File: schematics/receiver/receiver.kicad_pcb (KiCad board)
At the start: 4 copper layers, 30.6 x 67.9 mm, 28 parts, among them M1 Servo, M2 Motor, Q1 2N7000, Q2 2N7000, Q3 2N7000, Q4 2N7000, SW1 SW_Nidec_CAS-120A1, U1 PIC16F18324-xSL, U2 LM2937xT, U3 NRF24L01_Breakout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

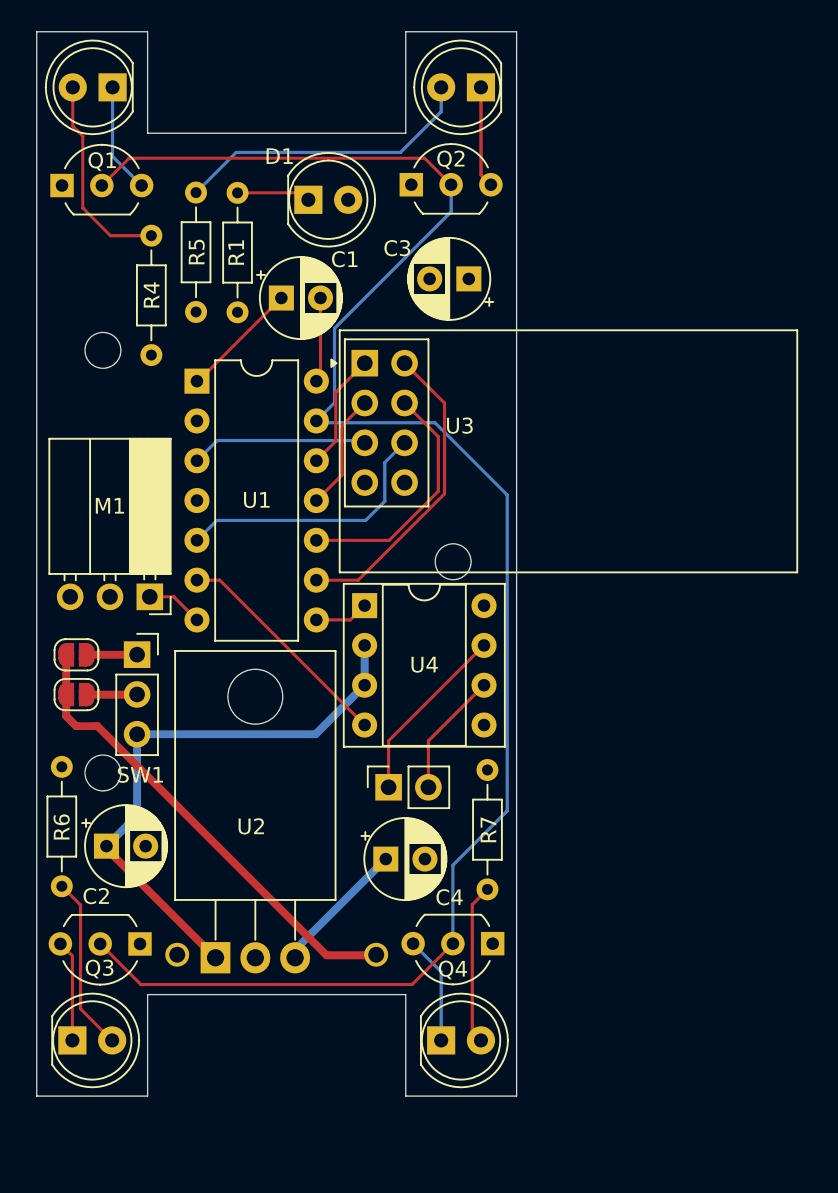
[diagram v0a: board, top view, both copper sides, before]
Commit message: Change mcu type select to be pull down for RX board
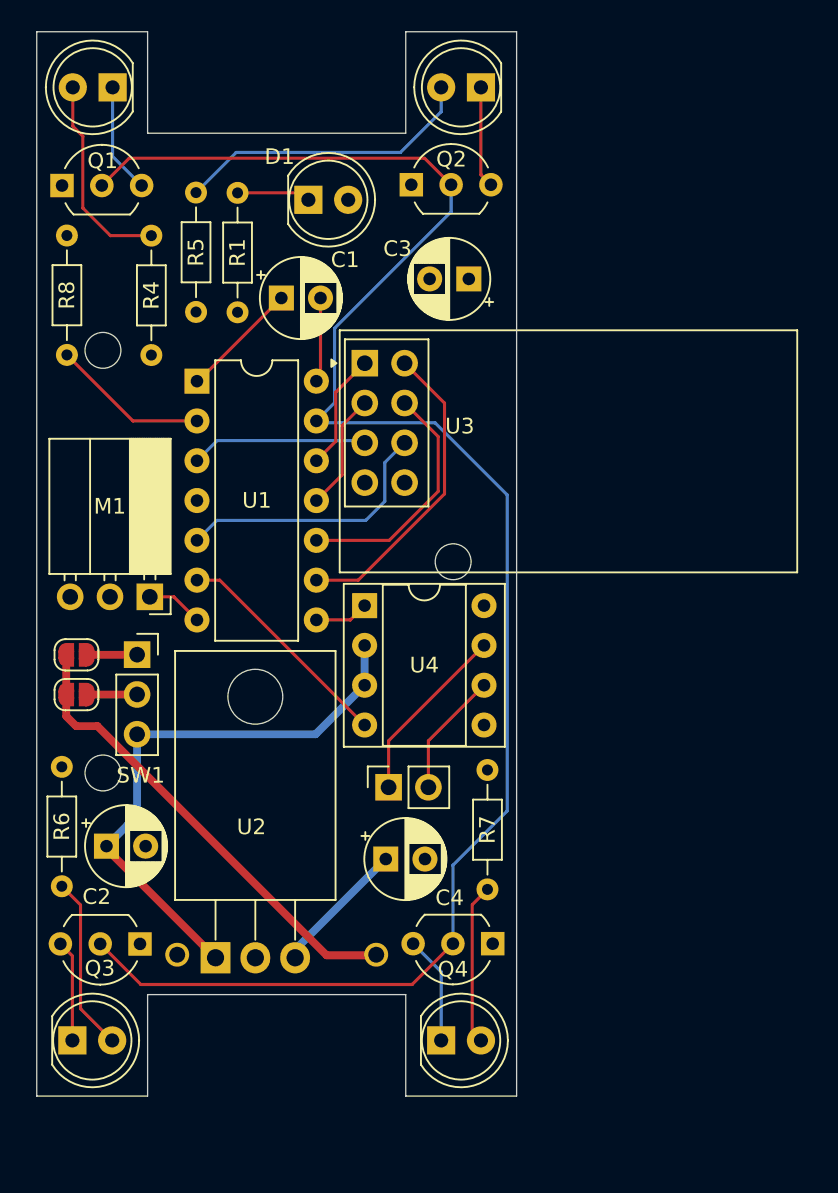
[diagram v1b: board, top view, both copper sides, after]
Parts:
- added R8: 10k, Resistor_THT:R_Axial_DIN0204_L3.6mm_D1.6mm_P7.62mm_Horizontal, F.Cu at (119.7, 64.8)
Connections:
- U1 pad 2: GND -> Net-(U1-RA5)
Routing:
- net Net-(U1-RA5): track 0.00 -> 10.0 mm

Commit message: Remove rear LEDs and move hbridge away from radio
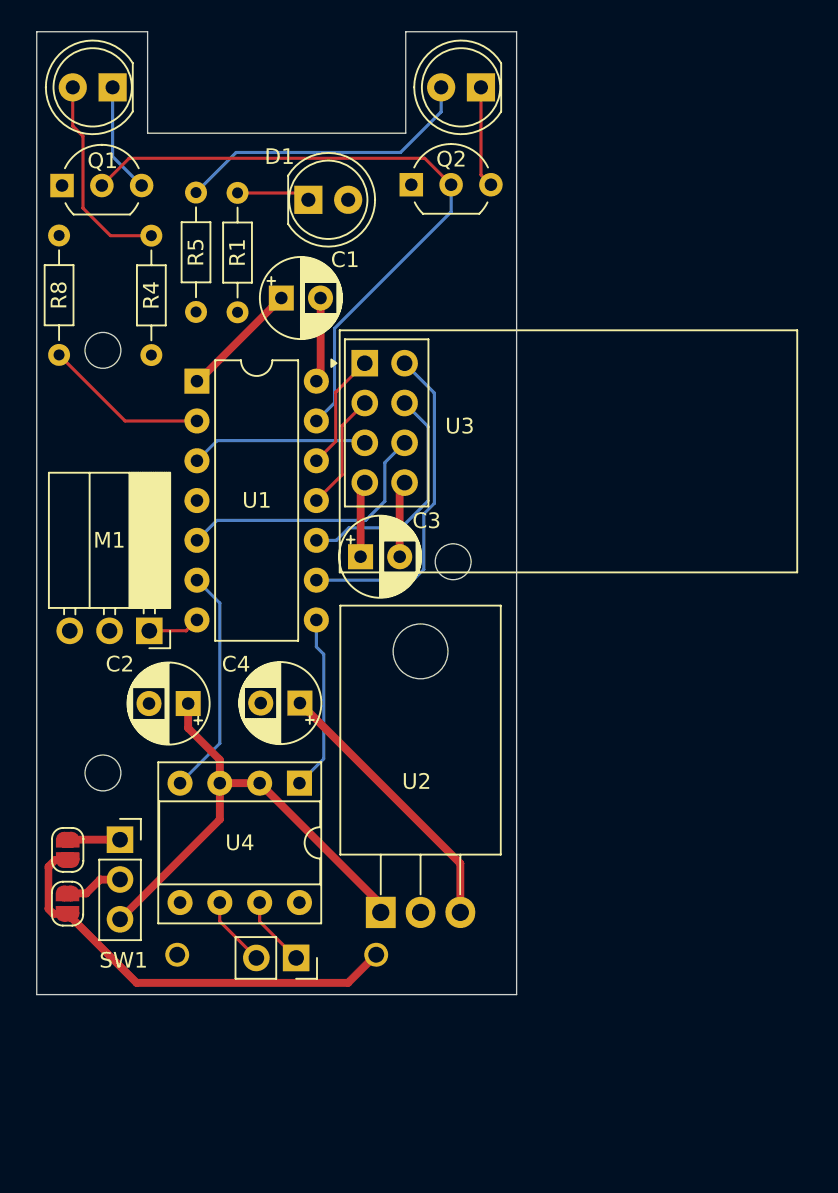
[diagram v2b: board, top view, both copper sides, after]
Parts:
- removed D4, D5: LED, LED_THT:LED_D5.0mm
- removed Q3, Q4: 2N7000, Package_TO_SOT_THT:TO-92_Inline_Wide
- removed R6, R7: 470, Resistor_THT:R_Axial_DIN0204_L3.6mm_D1.6mm_P7.62mm_Horizontal
- moved C3 19.0 mm to (138.4, 77.7), turned to 0 degrees
- moved JP1 13.4 mm to (119.7, 99.9), turned to 90 degrees
- moved JP2 12.5 mm to (119.8, 96.4), turned to 90 degrees
- moved M2 12.4 mm to (134.3, 103.3), turned to -90 degrees
- moved U4 12.1 mm to (134.5, 92.2), turned to -90 degrees
- moved SW1 11.9 mm to (123.1, 95.8)
- moved C4 11.4 mm to (134.6, 87.1), turned to 180 degrees
- moved U2 10.9 mm to (139.7, 100.4)
- moved C2 10.5 mm to (127.4, 87.1), turned to 180 degrees
- moved M1 2.17 mm to (125.0, 82.5)
- moved R8 0.50 mm to (119.2, 64.8)
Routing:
- net LIGHTS: track 111.2 -> 42.5 mm
- net +3.3V: track 16.9 -> 30.7 mm
- net Net-(D4-A): track 11.2 -> 0.00 mm
- net Net-(D5-A): track 10.3 -> 0.00 mm
- net PWM5: track 3.46 -> 11.3 mm
- net Net-(M2-+): track 11.6 -> 4.50 mm
- net Net-(D5-K): track 6.92 -> 0.00 mm
- net Net-(D4-K): track 6.48 -> 0.00 mm
- net +9V: track 36.3 -> 31.2 mm
- net GND: track 5.41 -> 10.3 mm
- net Net-(M2--): track 7.99 -> 4.50 mm
- net Net-(BT1-+): track 30.0 -> 27.7 mm
- net MISO: track 19.9 -> 21.4 mm
- net SCK: track 15.6 -> 15.0 mm
- net Net-(U1-RA5): track 10.0 -> 10.5 mm
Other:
- board size 30.6 x 67.9 mm -> 30.6 x 61.4 mm

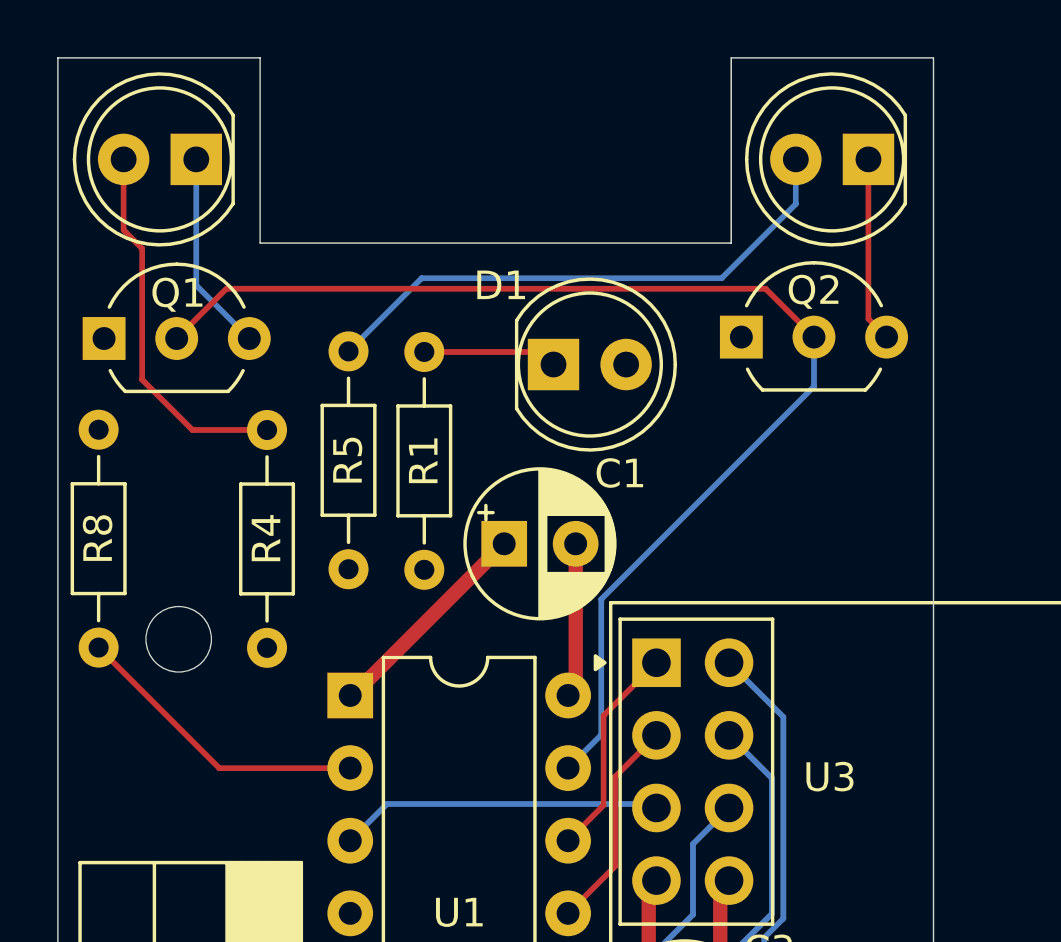
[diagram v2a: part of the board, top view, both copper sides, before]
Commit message: Rearrange for more room for screws
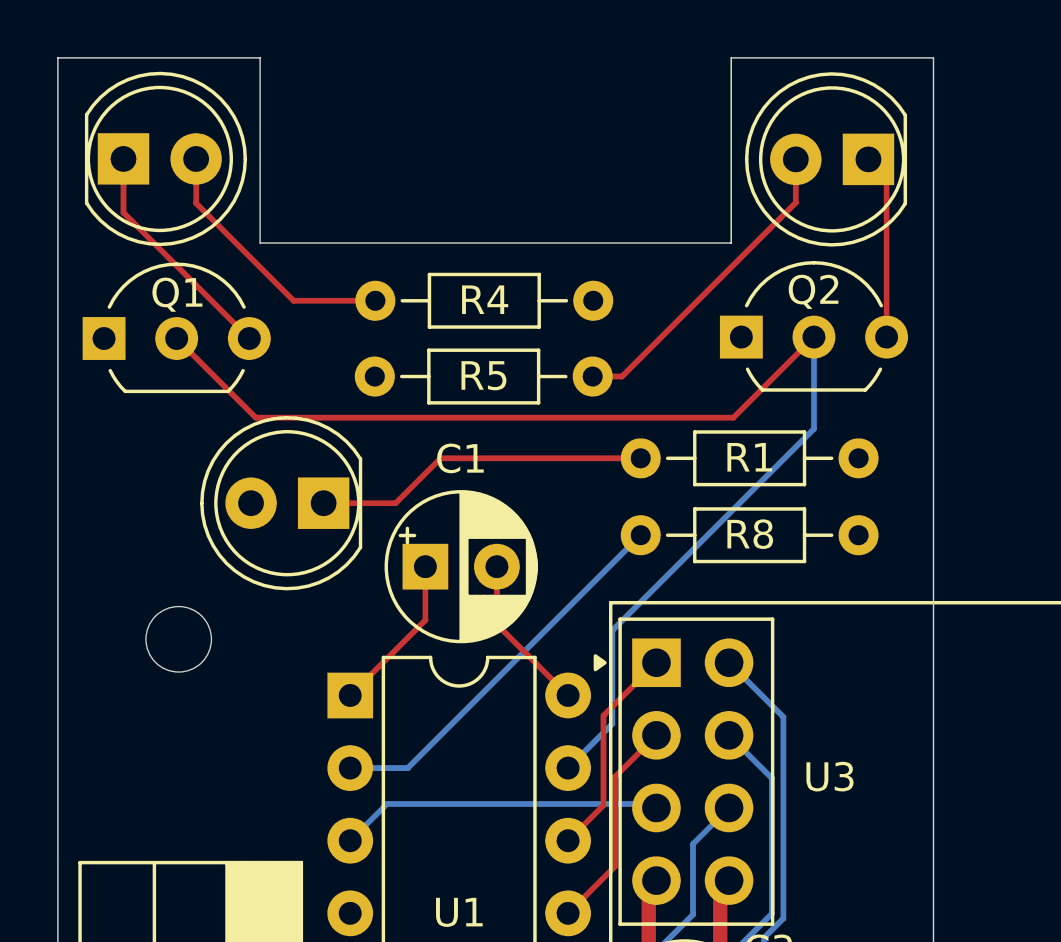
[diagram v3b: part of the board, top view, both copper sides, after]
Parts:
- moved R8 19.4 mm to (138.2, 60.9), turned to 0 degrees
- moved R4 16.7 mm to (136.5, 52.7), turned to 180 degrees
- moved D1 9.39 mm to (127.1, 59.8), turned to 180 degrees
- moved R1 8.43 mm to (138.2, 58.2), turned to 0 degrees
- moved R5 6.80 mm to (128.9, 55.4), turned to 0 degrees
- moved C1 2.87 mm to (130.6, 62.0)
- moved D2 2.55 mm to (120.1, 47.8), turned to 0 degrees
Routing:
- net Net-(D3-A): track 19.3 -> 11.1 mm
- net Net-(D1-K): track 5.52 -> 11.7 mm
- net Net-(D2-A): track 13.1 -> 9.23 mm
- net Net-(U1-RA5): track 10.5 -> 13.5 mm
- net +3.3V: track 30.7 -> 28.7 mm
- net Net-(D2-K): track 7.03 -> 8.10 mm
- net LIGHTS: track 42.5 -> 43.4 mm

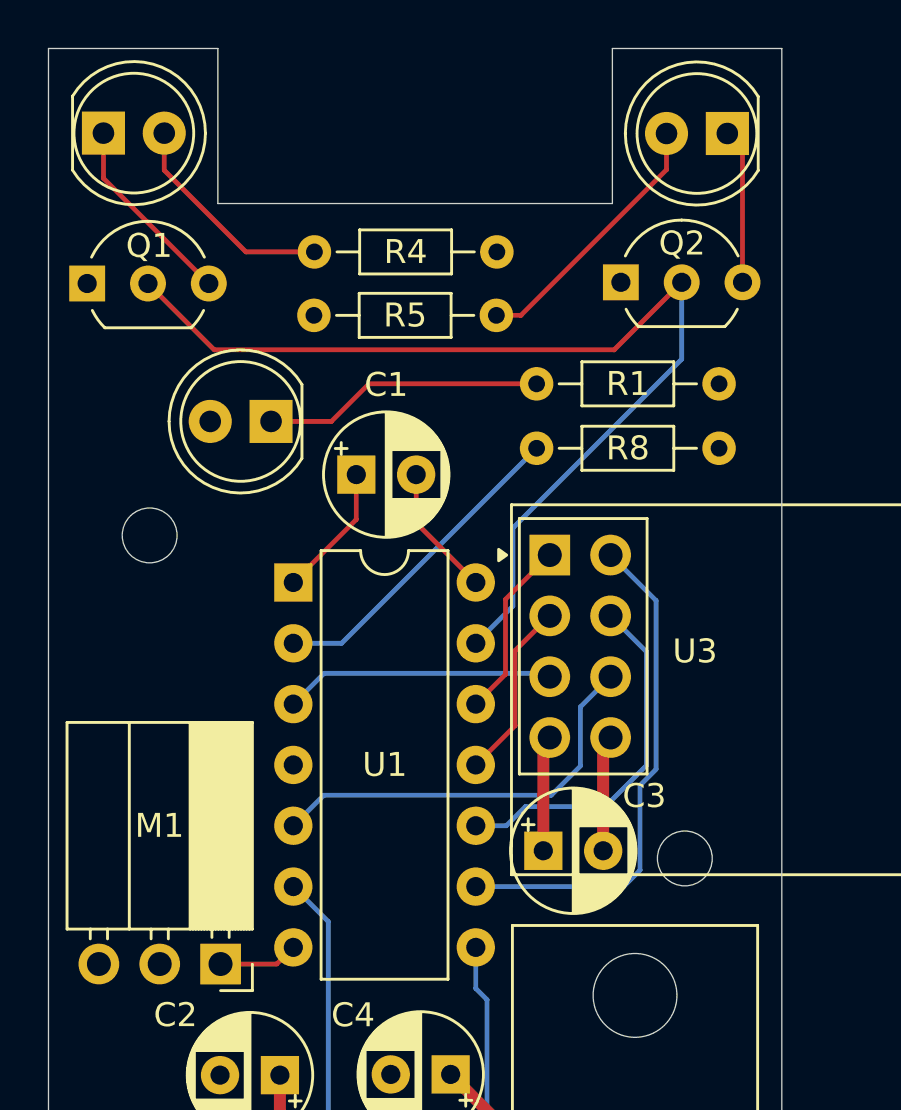
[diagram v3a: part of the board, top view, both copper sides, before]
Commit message: Add pull down resistor for LED control on receiver board
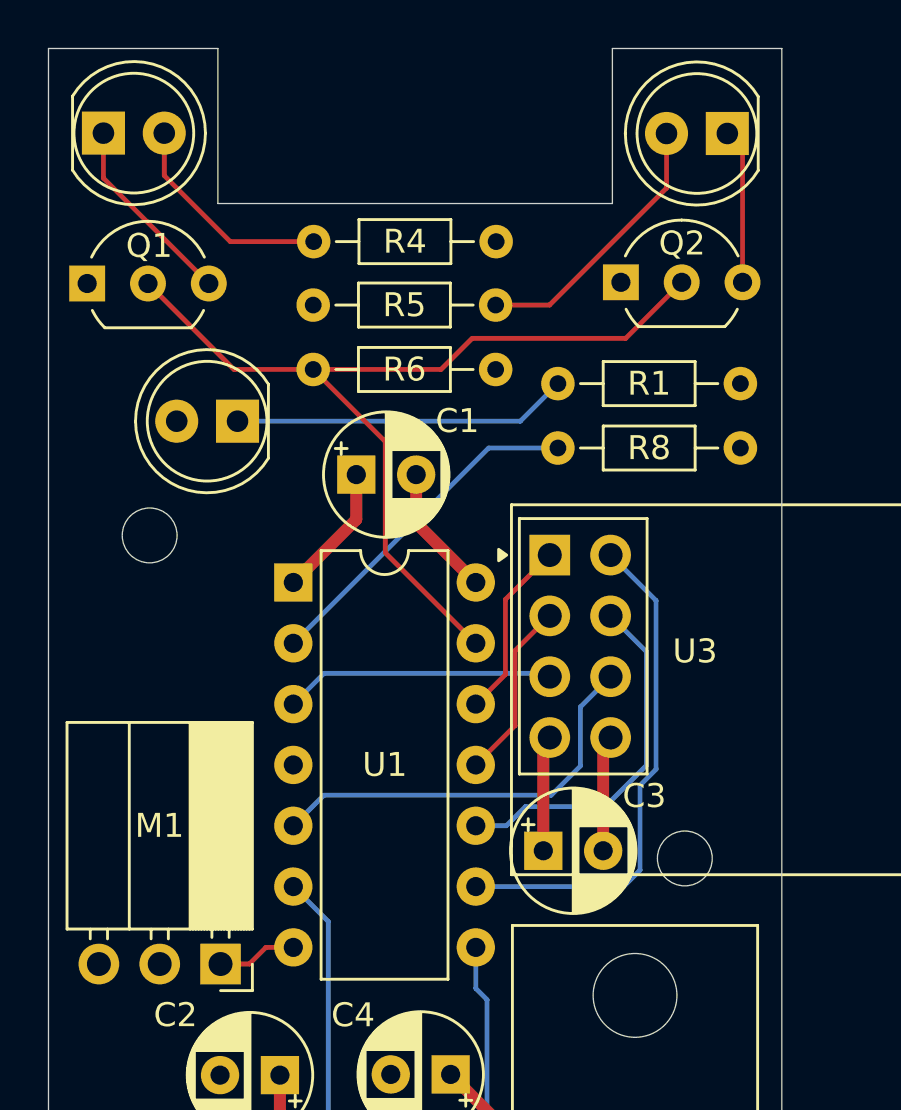
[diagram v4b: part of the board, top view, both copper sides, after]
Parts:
- added R6: 10k, Resistor_THT:R_Axial_DIN0204_L3.6mm_D1.6mm_P7.62mm_Horizontal, F.Cu at (128.8, 57.6)
- moved D1 1.40 mm to (125.7, 59.8)
- moved R1 0.89 mm to (139.1, 58.2)
- moved R8 0.89 mm to (139.1, 60.9)
- moved R4 0.43 mm to (136.5, 52.3)
- moved R5 0.43 mm to (128.8, 54.9)
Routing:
- net LIGHTS: track 43.4 -> 39.7 mm
- net Net-(D1-K): track 11.7 -> 14.0 mm
- net Net-(U1-RA5): track 13.5 -> 14.4 mm
